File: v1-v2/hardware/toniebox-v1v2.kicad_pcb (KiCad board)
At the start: 2 copper layers, 88 x 102 mm, 11 parts, among them T11 FDV301N, T4 FDV301N, T5 FDV301N, T6 FDV301N, T7 FDV301N, U1 TLV320DAC3100, U2 CC3200R1M2RGCR, U3 IS25LQ032B-JNLE, U4 MMA8451QT, U8 AP2112K-3.3, U9 AP2120N-1.8

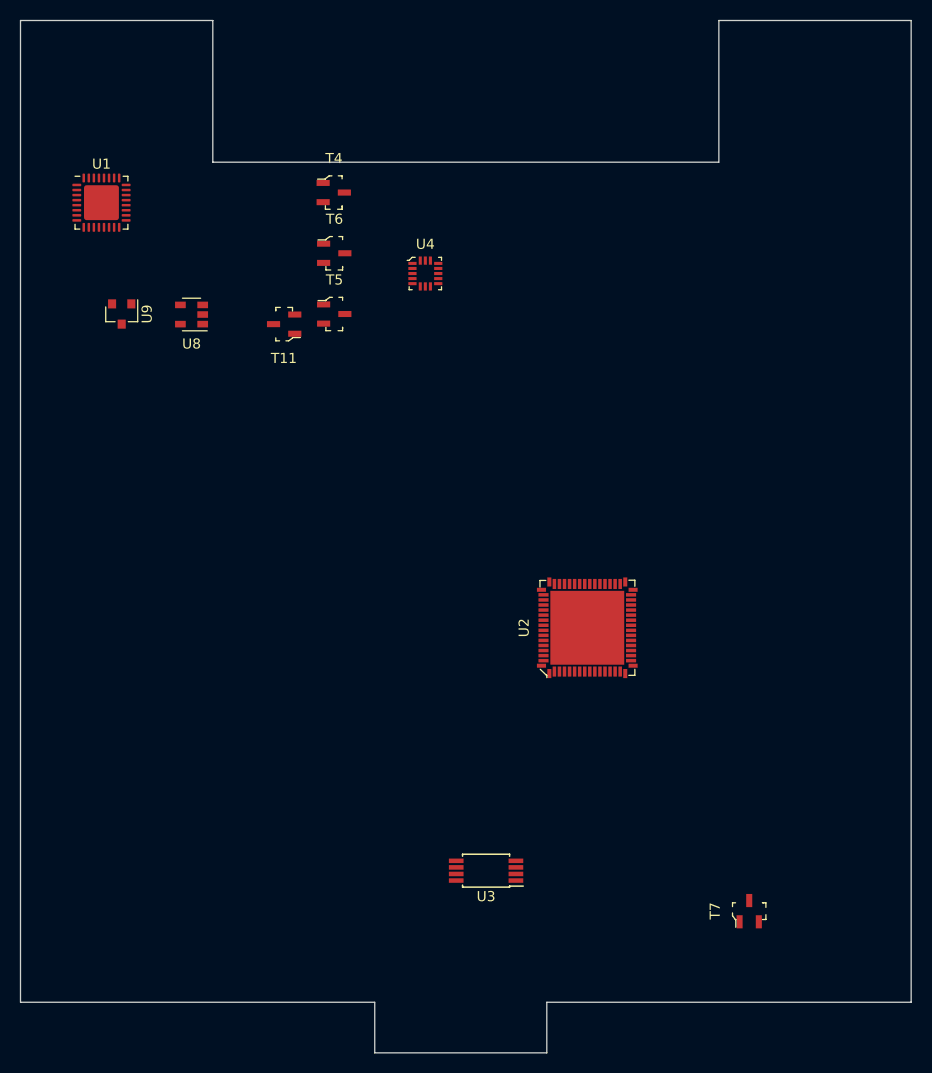
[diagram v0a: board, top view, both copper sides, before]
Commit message: Chg - KiCAD upgrade, More components
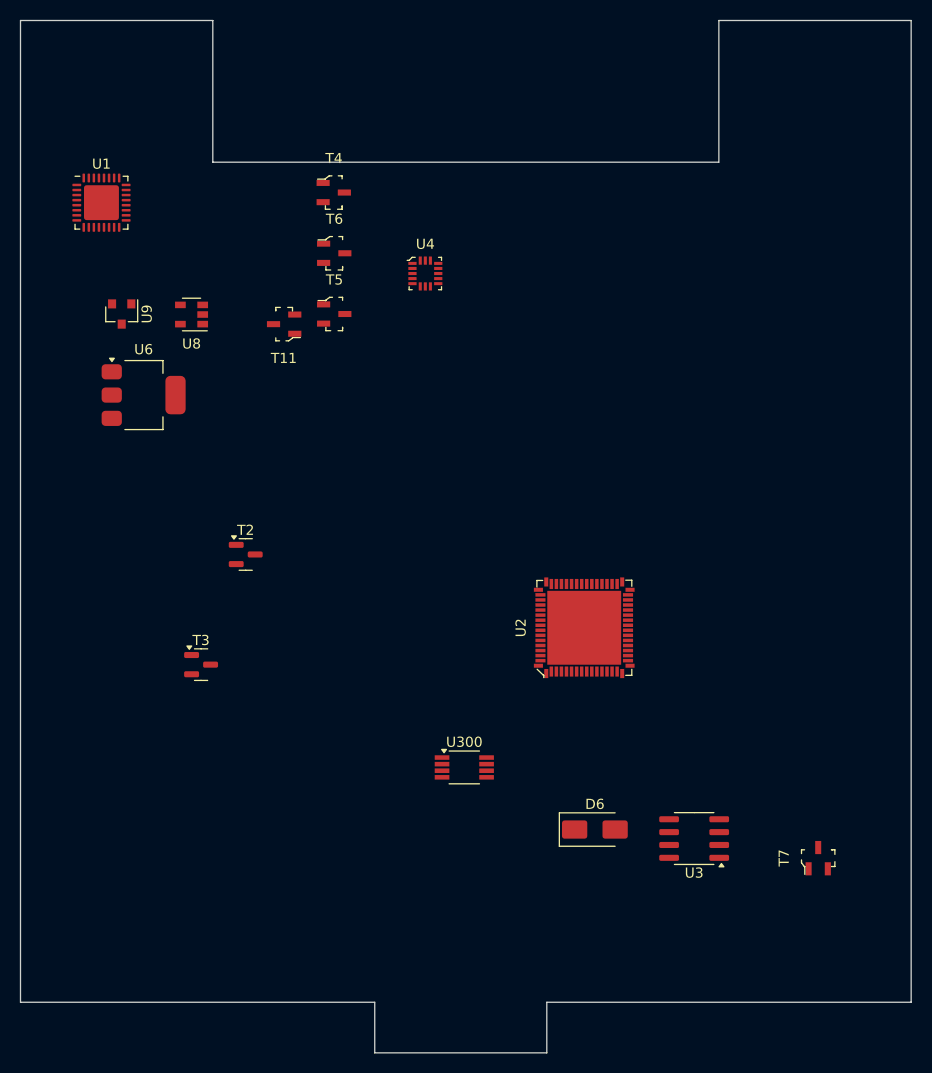
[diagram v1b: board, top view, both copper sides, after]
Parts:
- added D6: SS14, Diode_SMD:D_SMA, F.Cu at (156.8, 122.9)
- added T2: MMBT3904, Package_TO_SOT_SMD:SOT-23, F.Cu at (122.3, 95.8)
- added T3: MMBT3904, Package_TO_SOT_SMD:SOT-23, F.Cu at (117.8, 106.6)
- added U300: LM3485MM, Package_SO:VSSOP-8_3.0x3.0mm_P0.65mm, F.Cu at (143.8, 116.8)
- added U6: AP2114H-3.3TRG1, Package_TO_SOT_SMD:SOT-223-3_TabPin2, F.Cu at (112.2, 80.0)
- U3: footprint Package_SO:TSSOP-8_4.4x3mm_P0.65mm -> Package_SO:SOIC-8_3.9x4.9mm_P1.27mm
- moved U3 20.8 mm to (166.6, 123.8)
- moved T7 8.59 mm to (178.8, 125.8)
- moved U2 0.30 mm to (155.7, 103.0)
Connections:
- net Net-(U2-Pad1) renamed /SD_CLK
- net Net-(U2-Pad2) renamed /SD_CMD
- net Net-(U2-Pad64) renamed /SD_DAT0
- U1 pad 10: Net-(U1-Pad10) -> /I2C_SCL
- U1 pad 11: Net-(U1-Pad11) -> unconnected-(U1-VOL/MICDET-Pad11)
- U1 pad 12: Net-(U1-Pad12) -> unconnected-(U1-MICBIAS-Pad12)
- U1 pad 13: Net-(U1-Pad13) -> unconnected-(U1-AIN1-Pad13)
- U1 pad 14: Net-(U1-Pad14) -> unconnected-(U1-AIN2-Pad14)
- U1 pad 15: Net-(U1-Pad15) -> unconnected-(U1-NC-Pad15)
- U1 pad 16: Net-(U1-Pad16) -> unconnected-(U1-AVSS-Pad16)
- U1 pad 17: Net-(U1-Pad17) -> unconnected-(U1-AVDD-Pad17)
- U1 pad 18: Net-(U1-Pad18) -> unconnected-(U1-DVSS-Pad18)
- U1 pad 19: Net-(U1-Pad19) -> unconnected-(U1-SPKM-Pad19)
- U1 pad 20: Net-(U1-Pad20) -> unconnected-(U1-SPKVSS-Pad20)
- U1 pad 21: Net-(U1-Pad21) -> unconnected-(U1-SPKVDD-Pad21)
- U1 pad 22: Net-(U1-Pad22) -> unconnected-(U1-SPKP-Pad22)
- U1 pad 23: Net-(U1-Pad23) -> unconnected-(U1-SPKM-Pad23)
- U1 pad 24: Net-(U1-Pad24) -> unconnected-(U1-SPKVDD-Pad24)
- U1 pad 25: Net-(U1-Pad25) -> unconnected-(U1-SPKVSS-Pad25)
- U1 pad 26: Net-(U1-Pad26) -> unconnected-(U1-SPKP-Pad26)
- U1 pad 27: Net-(U1-Pad27) -> unconnected-(U1-HPL-Pad27)
- U1 pad 28: Net-(U1-Pad28) -> unconnected-(U1-HPVDD-Pad28)
- U1 pad 29: Net-(U1-Pad29) -> unconnected-(U1-HPVSS-Pad29)
- U1 pad 3: Net-(U1-Pad3) -> unconnected-(U1-DVDD-Pad3)
- U1 pad 30: Net-(U1-Pad30) -> unconnected-(U1-HPR-Pad30)
- U1 pad 32: Net-(U1-Pad32) -> unconnected-(U1-GPIO1-Pad32)
- U1 pad 4: Net-(U1-Pad4) -> unconnected-(U1-NC-Pad4)
- U1 pad 5: Net-(U1-Pad5) -> unconnected-(U1-DIN-Pad5)
- U1 pad 6: Net-(U1-Pad6) -> unconnected-(U1-WCLK-Pad6)
- U1 pad 7: Net-(U1-Pad7) -> unconnected-(U1-BCLK-Pad7)
- U1 pad 8: Net-(U1-Pad8) -> unconnected-(U1-MCLK-Pad8)
- U1 pad 9: Net-(U1-Pad9) -> /I2C_SDA
- U2 pad 10: Net-(U2-Pad10) -> +3V3
- U2 pad 11: Net-(U2-Pad11) -> unconnected-(U2-FLASH_SPI_CLK-Pad11)
- U2 pad 12: Net-(U2-Pad12) -> unconnected-(U2-FLASH_SPI_DOUT-Pad12)
- U2 pad 13: Net-(U2-Pad13) -> unconnected-(U2-FLASH_SPI_DIN-Pad13)
- U2 pad 14: Net-(U2-Pad14) -> unconnected-(U2-FLASH_SPI_CS-Pad14)
- U2 pad 15: Net-(U2-Pad15) -> unconnected-(U2-GPIO22-Pad15)
- U2 pad 16: Net-(U2-Pad16) -> unconnected-(U2-TDI-Pad16)
- U2 pad 18: Net-(U2-Pad18) -> unconnected-(U2-GPIO28-Pad18)
- U2 pad 22: Net-(U2-Pad22) -> unconnected-(U2-WLAN_XTAL_N-Pad22)
- U2 pad 23: Net-(U2-Pad23) -> unconnected-(U2-WLAN_XTAL_P-Pad23)
- U2 pad 24: Net-(U2-Pad24) -> unconnected-(U2-VDD_PLL-Pad24)
- U2 pad 25: Net-(U2-Pad25) -> unconnected-(U2-LDO_IN2-Pad25)
- U2 pad 26: Net-(U2-Pad26) -> unconnected-(U2-NC-Pad26)
- U2 pad 27: Net-(U2-Pad27) -> unconnected-(U2-NC-Pad27)
- U2 pad 28: Net-(U2-Pad28) -> unconnected-(U2-NC-Pad28)
- U2 pad 29: Net-(U2-Pad29) -> unconnected-(U2-ANTSEL1-Pad29)
- U2 pad 3: Net-(U2-Pad3) -> /I2C_SCL
- U2 pad 30: Net-(U2-Pad30) -> unconnected-(U2-ANTSEL2-Pad30)
- U2 pad 31: Net-(U2-Pad31) -> unconnected-(U2-RF_BG-Pad31)
- U2 pad 33: Net-(U2-Pad33) -> unconnected-(U2-VDD_PA_IN-Pad33)
- U2 pad 36: Net-(U2-Pad36) -> unconnected-(U2-LDO_IN1-Pad36)
- U2 pad 37: Net-(U2-Pad37) -> unconnected-(U2-VIN_DCDC_ANA-Pad37)
- U2 pad 38: Net-(U2-Pad38) -> unconnected-(U2-DCDC_ANA_SW-Pad38)
- U2 pad 39: Net-(U2-Pad39) -> unconnected-(U2-VIN_DCDC_PA-Pad39)
- U2 pad 4: Net-(U2-Pad4) -> /I2C_SDA
- U2 pad 40: Net-(U2-Pad40) -> unconnected-(U2-DCDC_PA_S_W_P-Pad40)
- U2 pad 41: Net-(U2-Pad41) -> unconnected-(U2-DCDC_PA_S_W_N-Pad41)
- U2 pad 42: Net-(U2-Pad42) -> unconnected-(U2-DCDC_PA_O_UT-Pad42)
- U2 pad 43: Net-(U2-Pad43) -> unconnected-(U2-DCDC_DIG_SW-Pad43)
- U2 pad 44: Net-(U2-Pad44) -> unconnected-(U2-VIN_DCDC_DIG-Pad44)
- U2 pad 46: Net-(U2-Pad46) -> unconnected-(U2-DCDC_ANA2_SW_N-Pad46)
- U2 pad 47: Net-(U2-Pad47) -> unconnected-(U2-VDD_ANA2-Pad47)
- U2 pad 48: Net-(U2-Pad48) -> unconnected-(U2-VDD_ANA1-Pad48)
- U2 pad 49: Net-(U2-Pad49) -> unconnected-(U2-VDD_RAM-Pad49)
- U2 pad 5: Net-(U2-Pad5) -> unconnected-(U2-GPIO14-Pad5)
- U2 pad 50: Net-(U2-Pad50) -> unconnected-(U2-GPIO0-Pad50)
- U2 pad 51: Net-(U2-Pad51) -> unconnected-(U2-RTC_XTAL_P-Pad51)
- U2 pad 52: Net-(U2-Pad52) -> unconnected-(U2-RTC_XTAL_N-Pad52)
- U2 pad 53: Net-(U2-Pad53) -> unconnected-(U2-GPIO30-Pad53)
- U2 pad 54: Net-(U2-Pad54) -> unconnected-(U2-VIN_IO2-Pad54)
- U2 pad 56: Net-(U2-Pad56) -> unconnected-(U2-VDD_DIG2-Pad56)
- U2 pad 58: Net-(U2-Pad58) -> unconnected-(U2-GPIO3-Pad58)
- U2 pad 59: Net-(U2-Pad59) -> unconnected-(U2-GPIO4-Pad59)
- U2 pad 6: Net-(U2-Pad6) -> unconnected-(U2-GPIO15-Pad6)
- U2 pad 60: Net-(U2-Pad60) -> unconnected-(U2-GPIO5-Pad60)
- U2 pad 62: Net-(U2-Pad62) -> unconnected-(U2-GPIO7-Pad62)
- U2 pad 63: Net-(U2-Pad63) -> unconnected-(U2-GPIO8-Pad63)
- U2 pad 65: Net-(U2-Pad65) -> unconnected-(U2-GND/TAB-Pad65)
- U2 pad 7: Net-(U2-Pad7) -> unconnected-(U2-GPIO16-Pad7)
- U2 pad 8: Net-(U2-Pad8) -> unconnected-(U2-GPIO17-Pad8)
- U2 pad 9: Net-(U2-Pad9) -> unconnected-(U2-VDD_DIG1-Pad9)
- U3 pad 1: Net-(U3-Pad1) -> unconnected-(U3-~{CE}-Pad1)
- U3 pad 4: Net-(U3-Pad4) -> unconnected-(U3-GND-Pad4)
- U3 pad 5: Net-(U3-Pad5) -> unconnected-(U3-SI/IO0-Pad5)
- U3 pad 6: Net-(U3-Pad6) -> unconnected-(U3-SCK-Pad6)
- U3 pad 8: Net-(U3-Pad8) -> unconnected-(U3-VCC-Pad8)
- U4 pad 10: Net-(U4-Pad10) -> unconnected-(U4-GND-Pad10)
- U4 pad 11: Net-(U4-Pad11) -> unconnected-(U4-INT1-Pad11)
- U4 pad 12: Net-(U4-Pad12) -> unconnected-(U4-GND-Pad12)
- U4 pad 13: Net-(U4-Pad13) -> unconnected-(U4-NC-Pad13)
- U4 pad 14: Net-(U4-Pad14) -> unconnected-(U4-VDD-Pad14)
- U4 pad 15: Net-(U4-Pad15) -> unconnected-(U4-NC-Pad15)
- U4 pad 16: Net-(U4-Pad16) -> unconnected-(U4-NC-Pad16)
- U4 pad 2: Net-(U4-Pad2) -> unconnected-(U4-BYP-Pad2)
- U4 pad 3: Net-(U4-Pad3) -> unconnected-(U4-DNC-Pad3)
- U4 pad 4: Net-(U4-Pad4) -> /I2C_SCL
- U4 pad 5: Net-(U4-Pad5) -> unconnected-(U4-GND-Pad5)
- U4 pad 6: Net-(U4-Pad6) -> /I2C_SDA
- U4 pad 7: Net-(U4-Pad7) -> GND
- U4 pad 8: Net-(U4-Pad8) -> unconnected-(U4-NC-Pad8)
- U4 pad 9: Net-(U4-Pad9) -> unconnected-(U4-INT2-Pad9)
- U8 pad 1: Net-(U8-Pad1) -> unconnected-(U8-VIN-Pad1)
- U8 pad 2: Net-(U8-Pad2) -> unconnected-(U8-GND-Pad2)
- U8 pad 4: Net-(U8-Pad4) -> unconnected-(U8-NC-Pad4)
- U9 pad 1: Net-(U9-Pad1) -> unconnected-(U9-GND-Pad1)
- U9 pad 2: Net-(U9-Pad2) -> unconnected-(U9-VO-Pad2)
- U9 pad 3: Net-(U9-Pad3) -> unconnected-(U9-VI-Pad3)
